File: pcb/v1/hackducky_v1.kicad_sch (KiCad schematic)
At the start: 34 parts, among them J1 USB_C_Receptacle_USB2.0_16P, J4 Micro_SD_Card, SW1 SW_Push, U1 XC6206PxxxMR, U2 W25Q64JVZPIQ, U3 RP2040, Y1 Crystal_GND23

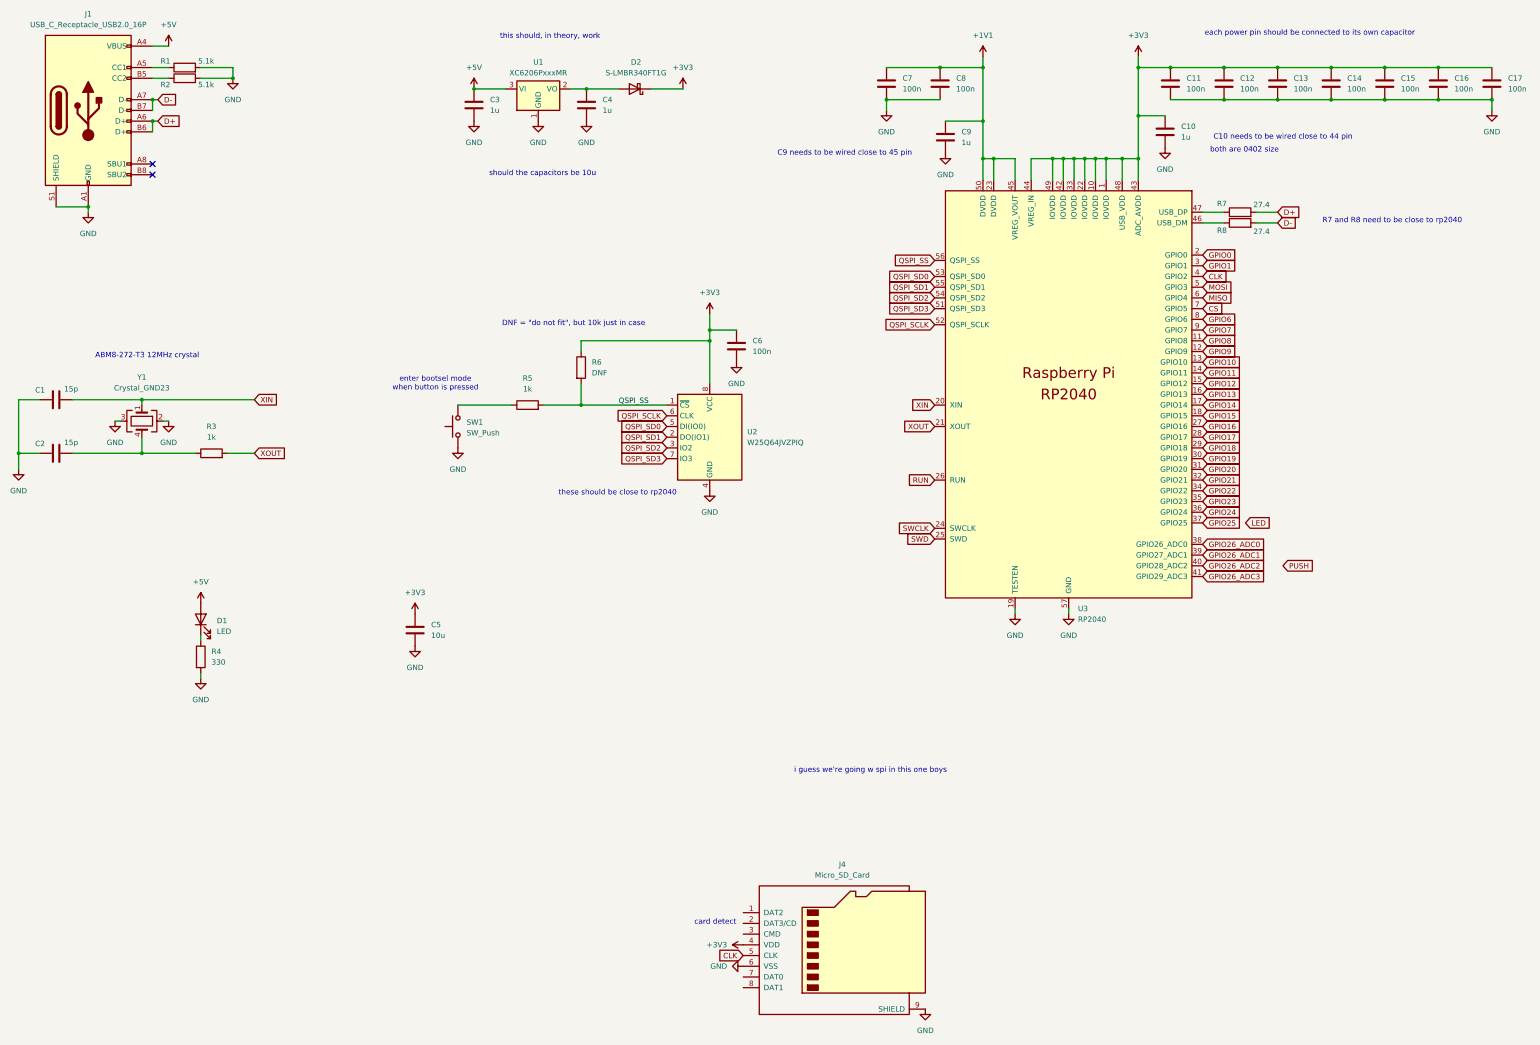
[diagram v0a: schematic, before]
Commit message: updated schematic, started pcb
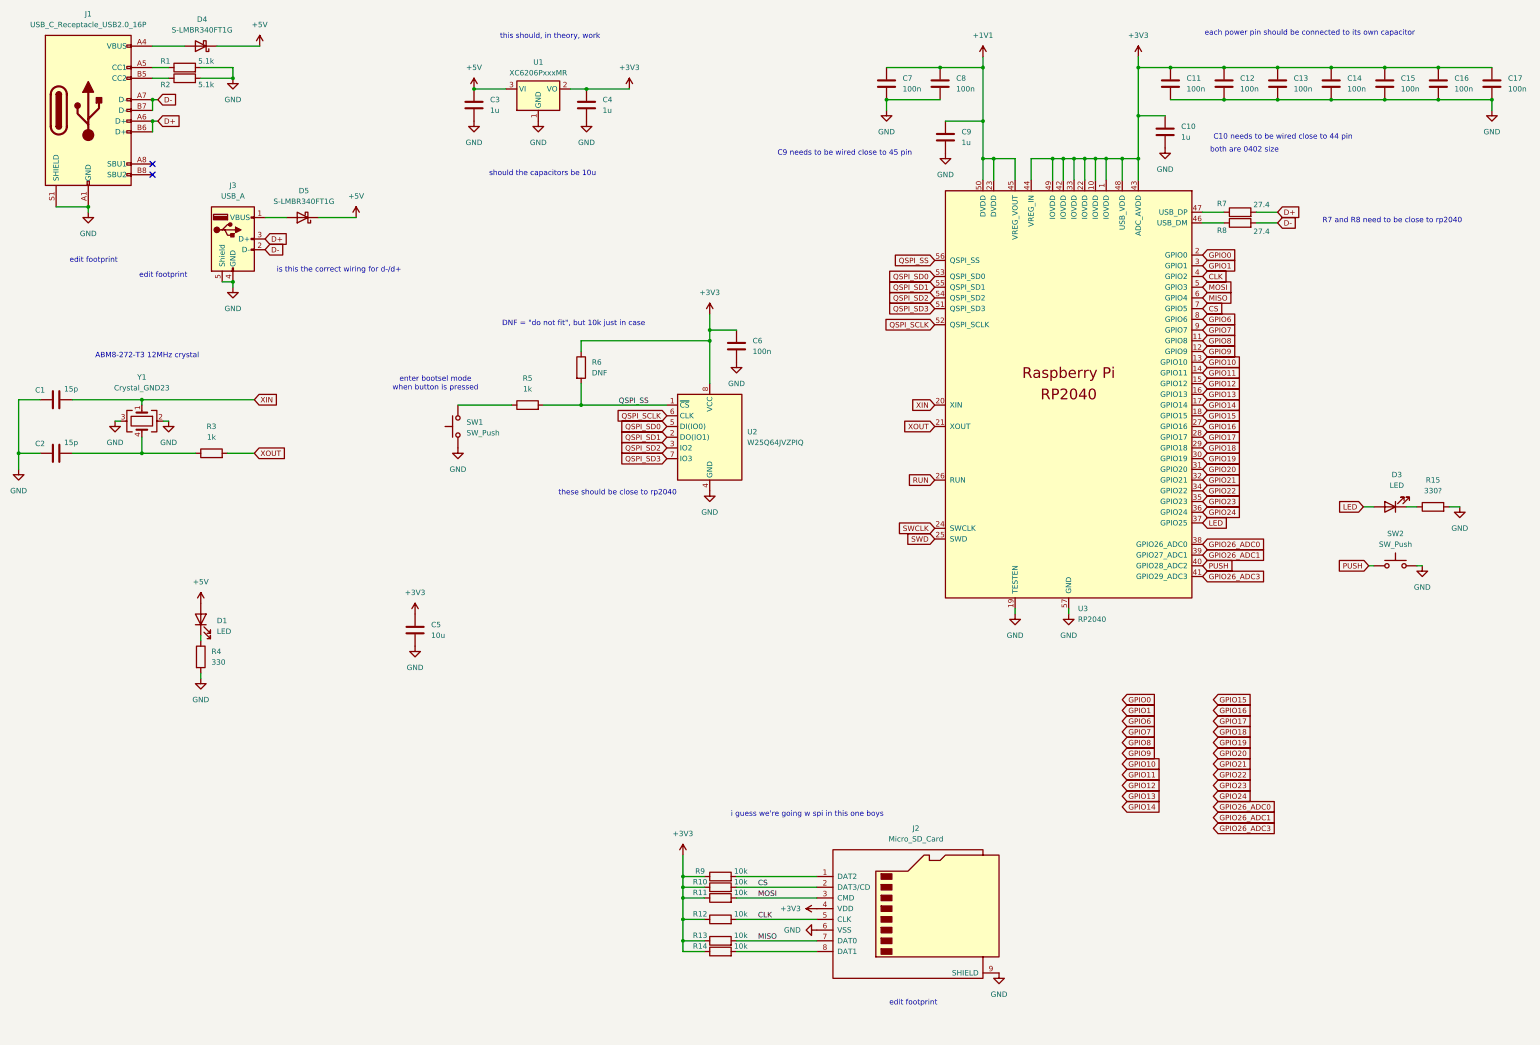
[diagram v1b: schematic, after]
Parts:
- removed D2: S-LMBR340FT1G, Diode_SMD:D_0805_2012Metric, symbol Device:D_Schottky
- removed J4: Micro_SD_Card, symbol Connector:Micro_SD_Card
- added D3: LED, LED_SMD:LED_0402_1005Metric, symbol Device:LED
- added D4, D5: S-LMBR340FT1G, Diode_SMD:D_0805_2012Metric, symbol Device:D_Schottky
- added J2: Micro_SD_Card, Connector_Card:microSD_HC_Molex_47219-2001, symbol Connector:Micro_SD_Card
- added J3: USB_A, Connector_USB:USB3_A_Plug_Wuerth_692112030100_Horizontal, symbol Connector:USB_A
- added R10, R11, R12, R13, R14, R9: 10k, Resistor_SMD:R_0402_1005Metric, symbol Device:R
- added R15: 330?, Resistor_SMD:R_0402_1005Metric, symbol Device:R
- added SW2: SW_Push, Button_Switch_THT:SW_PUSH_6mm, symbol Switch:SW_Push
- J1: footprint Connector_USB:USB_C_Receptacle_HCTL_HC-TYPE-C-16P-01A -> Connector_USB:USB_C_Plug_Molex_105444
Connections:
- net GPIO25 is gone; now on net LED: U3.37 (GPIO25)
- net GPIO26_ADC2 is gone; now on net PUSH: U3.40 (GPIO28_ADC2)
- net +3V3: now also C4.1, U1.2 (VO), J2.4 (VDD), R10.1, R11.1, R12.1, R13.1, R14.1, R9.1
- net +5V: now also D4.1 (K), D5.1 (K); no longer J1.A4 (VBUS), J1.A9 (VBUS), J1.B4 (VBUS), J1.B9 (VBUS)
- net CLK: now also J2.5 (CLK), R12.2
- net CS: now also J2.2 (DAT3/CD), R10.2
- net D+: now also J3.3 (D+)
- net D-: now also J3.2 (D-)
- net GND: now also J2.6 (VSS), J2.9 (SHIELD), J3.4 (GND), J3.5 (Shield), R15.2, SW2.2
- net LED: now also D3.2 (A)
- net MISO: now also J2.7 (DAT0), R13.2
- net MOSI: now also J2.3 (CMD), R11.2
- net PUSH: now also SW2.1
- new net: J2.8 (DAT1), R14.2
- new net: J2.1 (DAT2), R9.2
- new net: D3.1 (K), R15.1
- new net: D5.2 (A), J3.1 (VBUS)
- new net: D4.2 (A), J1.A4 (VBUS), J1.A9 (VBUS), J1.B4 (VBUS), J1.B9 (VBUS)
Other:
- note added: "edit footprint"
- note added: "is this the correct wiring for d-/d+"
- note removed: "card detect"
